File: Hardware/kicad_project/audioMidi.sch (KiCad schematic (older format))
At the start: 26 parts

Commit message: update project with corrected schematic / pcb
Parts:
- removed U?: SPWmicrophone, RandomJunk:SPW2430HR5H-B, symbol customLibrary:SPWmicrophone
- added U4: AP3722AT_mic, RandomJunk:AP3722AT-SMD-mic, symbol customLibrary:AP3722AT_mic
- C38, C42, C43, C46, C50: renamed from C?; footprint RandomJunk:C_0603_nosilk -> Capacitors_SMD:C_0402_NoSilk; LCSC c19702 -> C15525
- C41: renamed from C?; value 1.0u -> 1u; footprint RandomJunk:C_0603_nosilk -> RandomJunk:C_0402_NoSilk
- R10, R12, R13: renamed from R?; footprint (none) -> Resistors_SMD:R_0402_NoSilk; LCSC (none) -> C25091
- R11: renamed from R?; footprint (none) -> Resistors_SMD:R_0402_NoSilk; LCSC (none) -> C11702
- R9: renamed from R?; footprint Resistors_SMD:R_0603 -> Resistors_SMD:R_0402_NoSilk; LCSC c23162 -> C23162
- U5: renamed from U?; footprint digikey-footprints:DIP-8_W7.62mm -> Housings_SOIC:SO-8_5.3x6.2mm_Pitch1.27mm; LCSC (none) -> C45303
- gave numbers to parts that had none: 13
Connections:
- wire segments 73 -> 75

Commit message: initial firmware commit, update hardware
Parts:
- R9: LCSC C23162 -> C25900
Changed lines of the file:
@@
 F 2 "Resistors_SMD:R_0402_NoSilk" V 2240 2590 50  0001 C CNN
 F 3 "~" H 2200 2600 50  0001 C CNN
-F 4 "C23162" H 2200 2600 50  0001 C CNN "LCSC"
+F 4 "C25900" H 2200 2600 50  0001 C CNN "LCSC"
 	1    2200 2600
 	0    1    1    0

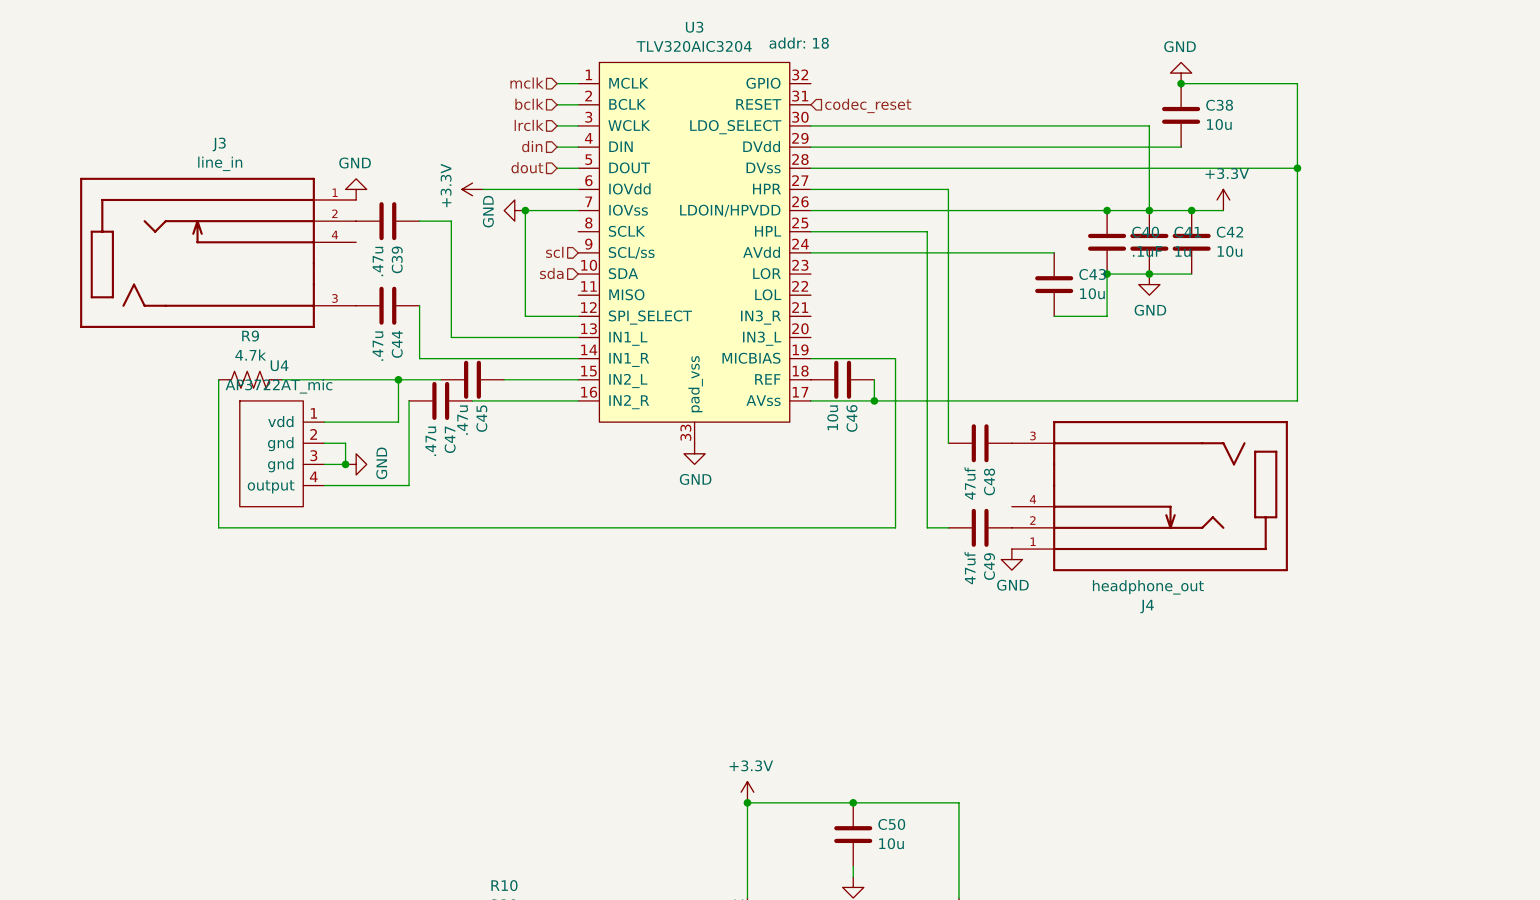
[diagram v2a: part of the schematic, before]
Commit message: new hardware rev
- soft / latching power switch
- corrected mic
- added pullup to flash ss
- front & back enclosure plates
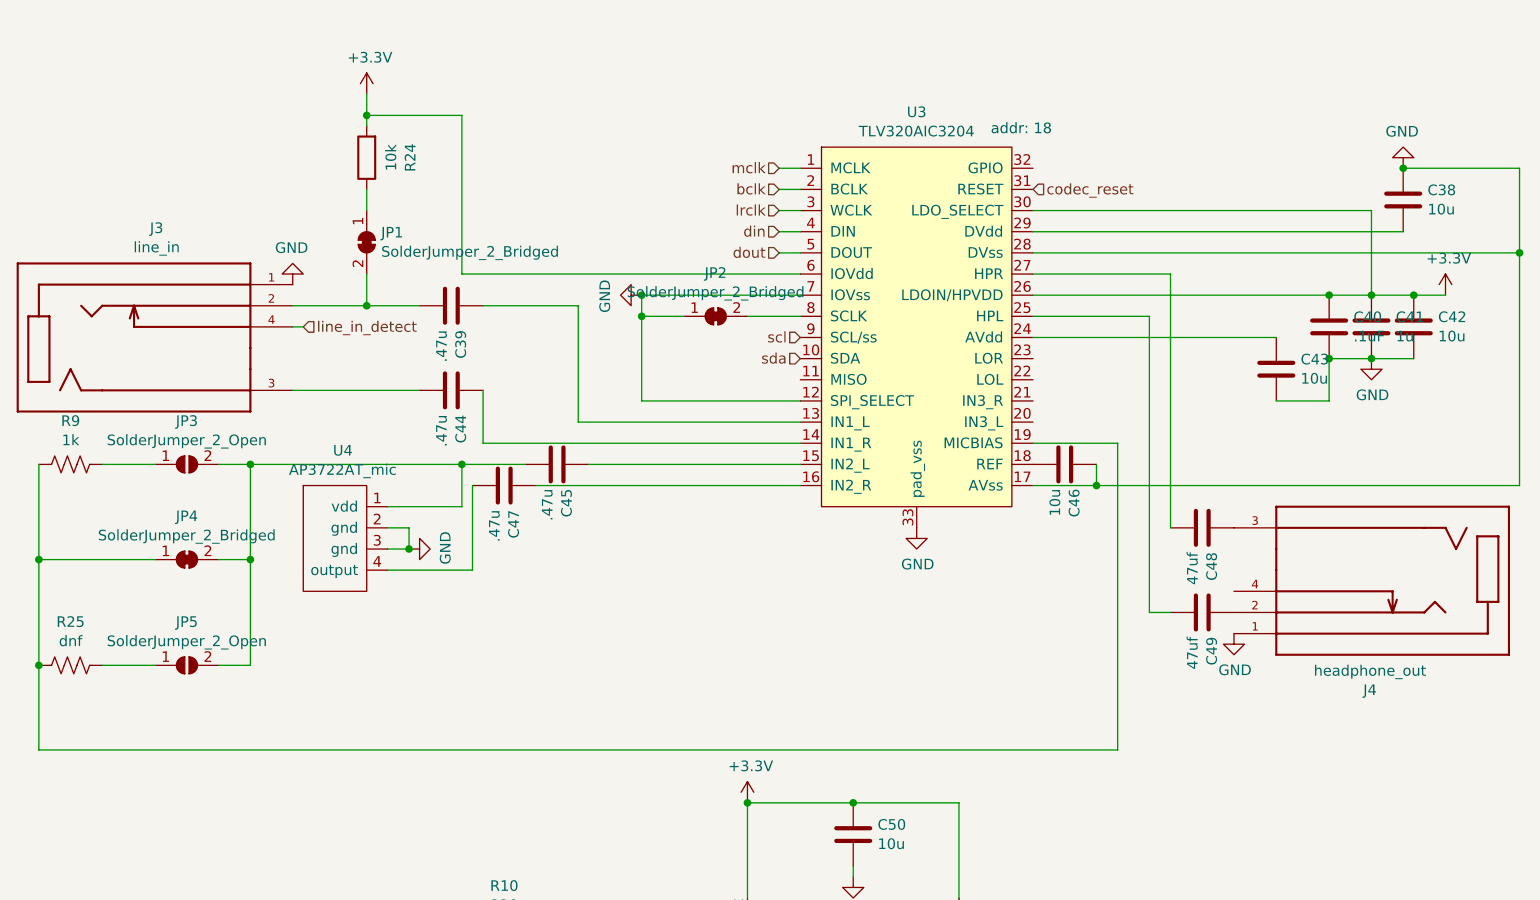
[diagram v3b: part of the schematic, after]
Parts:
- added JP1, JP2, JP4: SolderJumper_2_Bridged, Jumper:SolderJumper-2_P1.3mm_Bridged_RoundedPad1.0x1.5mm, symbol Jumper:SolderJumper_2_Bridged
- added JP3, JP5: SolderJumper_2_Open, Jumper:SolderJumper-2_P1.3mm_Open_RoundedPad1.0x1.5mm, symbol Jumper:SolderJumper_2_Open
- added R24: 10k, Resistors_SMD:R_0402_NoSilk, symbol Device:R
- added R25: dnf, Resistors_SMD:R_0805_HandSoldering, symbol Device:R_US
- C41: LCSC c15849 -> C52923
- R9: value 4.7k -> 1k; LCSC C25900 -> C11702
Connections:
- net +3V3: now also R24.2
- net GND: now also JP2.1 (A)
- net at C45.2, U4.1 (vdd): now also JP3.2 (B), JP4.2 (B), JP5.2 (B); no longer R9.1
- net at R9.2, U3.19 (MICBIAS): now also JP4.1 (A), R25.2
- net at U3.8 (SCLK): now also JP2.2 (B)
- net at C39.2, J3.2 (TIP_1): now also JP1.2 (B)
- net line_in_detect: now reaches J3.4 (TIP_SWITCH)
- new net: JP1.1 (A), R24.1
- new net: JP3.1 (A), R9.1
- new net: JP5.1 (A), R25.1
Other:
- moved on the sheet: C38, C39, C40, C41, C42, C43, C44, C45, C46, C47, C48, C49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

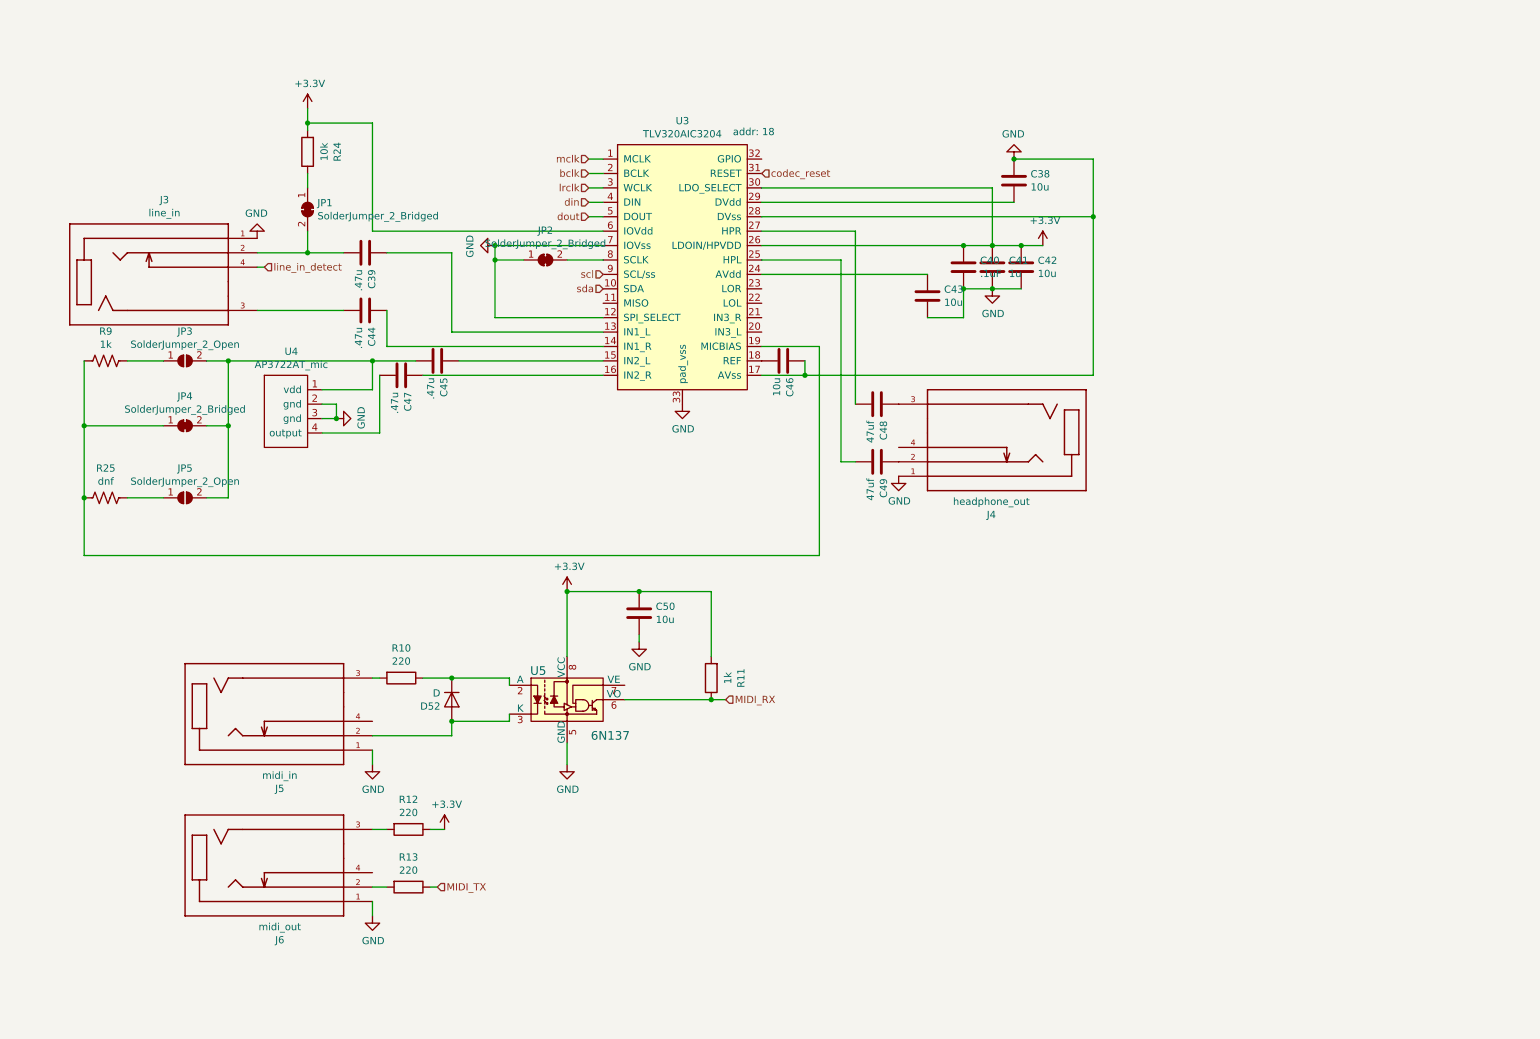
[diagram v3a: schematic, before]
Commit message: new hardware rev
reworked power system
added amp
new LDOS (less dropout)
dedicated LDO for audio system
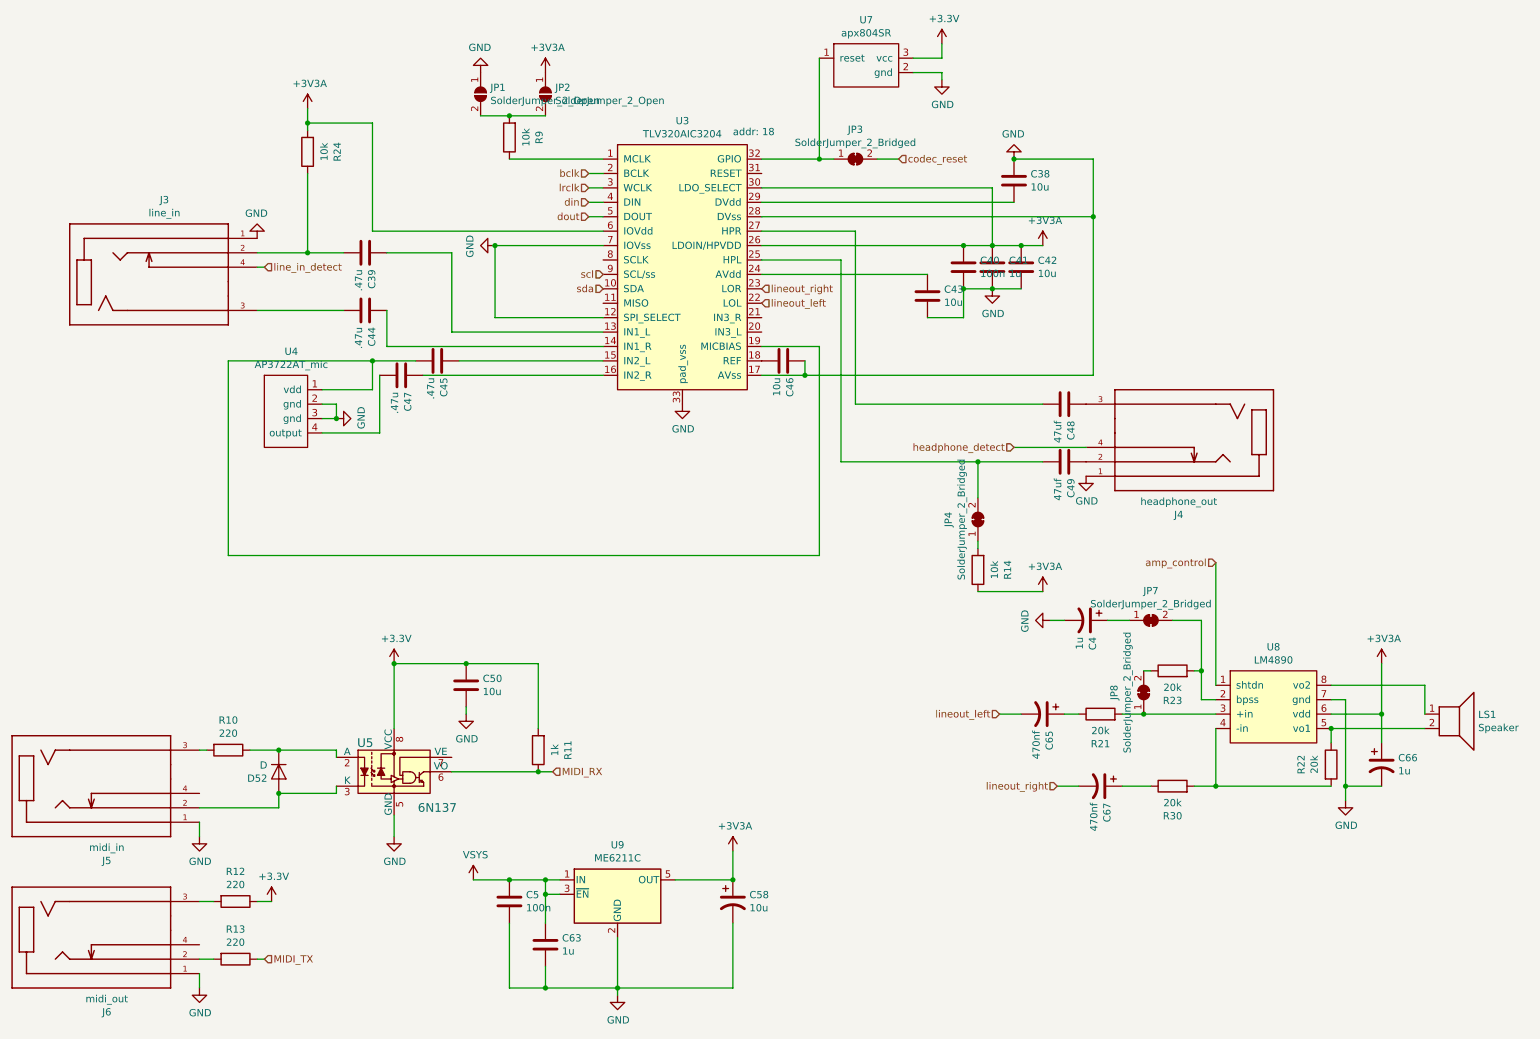
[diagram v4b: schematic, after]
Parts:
- removed JP1, JP2: SolderJumper_2_Bridged, Jumper:SolderJumper-2_P1.3mm_Bridged_RoundedPad1.0x1.5mm, symbol Jumper:SolderJumper_2_Bridged
- removed JP3, JP5: SolderJumper_2_Open, Jumper:SolderJumper-2_P1.3mm_Open_RoundedPad1.0x1.5mm, symbol Jumper:SolderJumper_2_Open
- removed R25: dnf, Resistors_SMD:R_0805_HandSoldering, symbol Device:R_US
- removed R9: 1k, Resistors_SMD:R_0402_NoSilk, symbol Device:R_US
- added C4, C66: 1u, Capacitors_Tantalum_SMD:CP_Tantalum_Case-A_EIA-3216-18_Reflow, symbol Device:CP1
- added C5: 100n, Capacitors_SMD:C_0402_NoSilk, symbol Device:C
- added C58: 10u, Capacitors_Tantalum_SMD:CP_Tantalum_Case-A_EIA-3216-18_Reflow, symbol Device:CP1
- added C63: 1u, Capacitors_SMD:C_0402_NoSilk, symbol Device:C
- added C65, C67: 470nf, Capacitors_Tantalum_SMD:CP_Tantalum_Case-A_EIA-3216-18_Reflow, symbol Device:CP1
- added JP1, JP2: SolderJumper_2_Open, Jumper:SolderJumper-2_P1.3mm_Open_RoundedPad1.0x1.5mm, symbol Jumper:SolderJumper_2_Open
- added JP3, JP7, JP8: SolderJumper_2_Bridged, Jumper:SolderJumper-2_P1.3mm_Bridged_Pad1.0x1.5mm, symbol Jumper:SolderJumper_2_Bridged
- added LS1: Speaker, Connector_PinHeader_2.54mm:PinHeader_1x02_P2.54mm_Horizontal, symbol Device:Speaker
- added R14, R9: 10k, Resistors_SMD:R_0402_NoSilk, symbol Device:R
- added R21, R22, R23, R30: 20k, Resistors_SMD:R_0402_NoSilk, symbol Device:R
- added U7: apx804SR, TO_SOT_Packages_SMD:SOT-23, symbol customLibrary:apx804SR
- added U8: LM4890, Housings_SSOP:MSOP-8_3x3mm_Pitch0.65mm, symbol customLibrary:fm8002a
- added U9: ME6211C, TO_SOT_Packages_SMD:SOT-23-5, symbol customLibrary:ME6211C
- C40: value .1uF -> 100n; footprint RandomJunk:C_0603_nosilk -> Capacitors_SMD:C_0402_NoSilk; LCSC c14663 -> C307331
- C41: footprint RandomJunk:C_0402_NoSilk -> Capacitors_SMD:C_0402_NoSilk
- JP4: footprint Jumper:SolderJumper-2_P1.3mm_Bridged_RoundedPad1.0x1.5mm -> Jumper:SolderJumper-2_P1.3mm_Bridged_Pad1.0x1.5mm; checked (none) -> 1
- U3: LCSC C24109 -> C9925
- U5: footprint Housings_SOIC:SO-8_5.3x6.2mm_Pitch1.27mm -> RandomJunk:SOP-8_3.9x5.1x1.27P; checked (none) -> 1
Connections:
- net +3V3: now also U7.3 (vcc); no longer C40.1, C41.1, C42.1, R24.2, U3.26 (LDOIN/HPVDD), U3.30 (LDO_SELECT), U3.6 (IOVdd)
- net GND: now also C4.2, C5.2, C58.2, C63.2, C66.2, JP1.1 (A), U7.2 (gnd), U8.7 (gnd), U9.2 (GND)
- net codec_reset: now also JP3.2 (B); no longer U3.31 (RESET)
- net at C45.2, U4.1 (vdd): now also U3.19 (MICBIAS); no longer JP4.2 (B)
- net at R24.1: now also C39.2, J3.2 (TIP_1)
- net at JP4.1 (A): now also R14.2; no longer U3.19 (MICBIAS)
- net headphone_detect: now reaches J4.4 (TIP_SWITCH)
- net lineout_left: now reaches U3.22 (LOL)
- net lineout_left: now also C65.2
- net lineout_right: now reaches U3.23 (LOR)
- net lineout_right: now also C67.2
- net at C49.2, U3.25 (HPL): now also JP4.2 (B)
- net at U3.32 (GPIO): now also JP3.1 (A), U7.1 (reset)
- net mclk: no longer names the net of U3.1 (MCLK)
- net mclk: now also R9.1
- new net: JP1.2 (B), JP2.2 (B), R9.2
- new net: JP7.2 (B), R23.2, U8.2 (bpss)
- new net: JP8.1 (A), R21.2, U8.3 (+in)
- new net: R22.2, R30.2, U8.4 (-in)
- new net: LS1.2, R22.1, U8.5 (vo1)
- new net: LS1.1, U8.8 (vo2)
- new net: C65.1, R21.1
- new net: C67.1, R30.1
- new net: JP8.2 (B), R23.1
- new net: C4.1, JP7.1 (A)
- new net +3V3A: C40.1, C41.1, C42.1, C58.1, C66.1, JP2.1 (A), R14.1, R24.2, U3.26 (LDOIN/HPVDD), U3.30 (LDO_SELECT), U3.6 (IOVdd), U8.6 (vdd), U9.5 (OUT)
- new net VBUS: C5.1, C63.1, U9.1 (IN), U9.3 (~EN~)
- new net amp_control: U8.1 (shtdn)
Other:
- moved on the sheet: C48, C49, C50, D52, J4, J5, J6, R10, R11, R12, R13, U5
